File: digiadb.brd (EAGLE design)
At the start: 18.2 x 19 mm, 3 parts

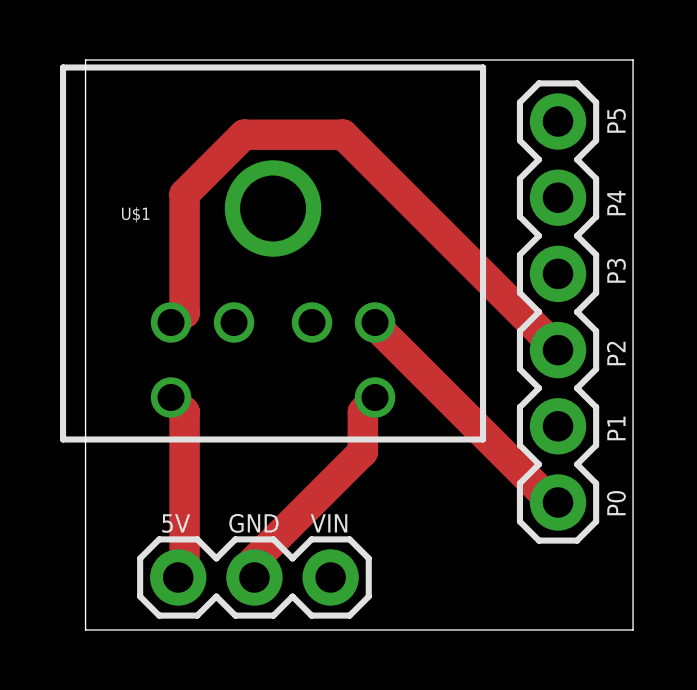
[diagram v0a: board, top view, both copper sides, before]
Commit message: added missing 470Ω pullup resistor from adb
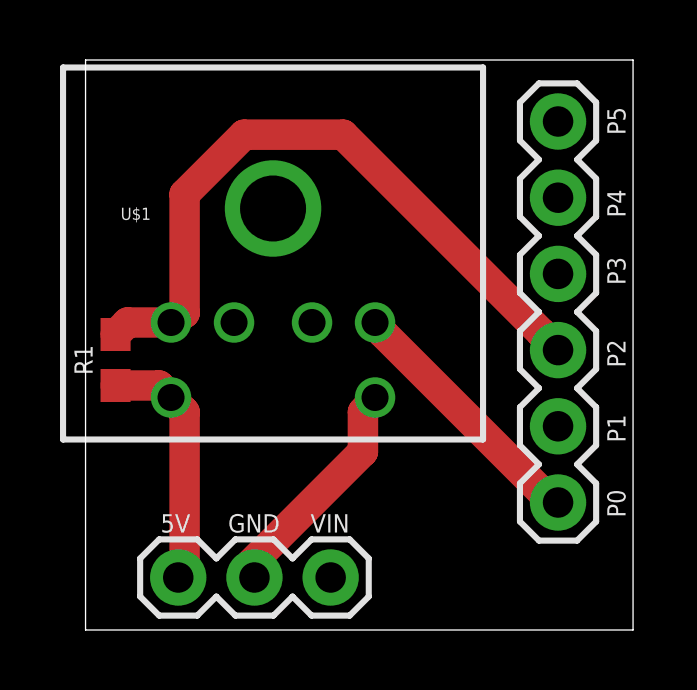
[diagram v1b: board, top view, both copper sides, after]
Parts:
- added R1: 470, SparkFun-Resistors:0603
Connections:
- net GND1 renamed GND
- net 5VCC: now also R1.1
- net ADB: now also R1.2
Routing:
- net 5VCC: track 6.26 -> 8.28 mm
- net ADB: track 20.8 -> 22.8 mm
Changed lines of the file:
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@@
 <?xml version="1.0" encoding="utf-8"?>
 <!DOCTYPE eagle SYSTEM "eagle.dtd">
-<eagle version="7.2.0">
+<eagle version="9.0.1">
 <drawing>
 <settings>
-<setting alwaysvectorfont="no"/>
+<setting alwaysvectorfont="yes"/>
+<setting keepoldvectorfont="yes"/>
 <setting verticaltext="up"/>
 </settings>
@@
 <layers>
 <layer number="1" name="Top" color="4" fill="1" visible="yes" active="yes"/>
+<layer number="2" name="Route2" color="1" fill="3" visible="yes" active="yes"/>
+<layer number="3" name="Route3" color="4" fill="3" visible="yes" active="yes"/>
+<layer number="4" name="Route4" color="1" fill="4" visible="yes" active="yes"/>
+<layer number="5" name="Route5" color="4" fill="4" visible="yes" active="yes"/>
+<layer number="6" name="Route6" color="1" fill="8" visible="yes" active="yes"/>
+<layer number="7" name="Route7" color="4" fill="8" visible="yes" active="yes"/>
+<layer number="8" name="Route8" color="1" fill="2" visible="yes" active="yes"/>
+<layer number="9" name="Route9" color="4" fill="2" visible="yes" active="yes"/>
+<layer number="10" name="Route10" color="1" fill="7" visible="yes" active="yes"/>
+<layer number="11" name="Route11" color="4" fill="7" visible="yes" active="yes"/>
+<layer number="12" name="Route12" color="1" fill="5" visible="yes" active="yes"/>
+<layer number="13" name="Route13" color="4" fill="5" visible="yes" active="yes"/>
+<layer number="14" name="Route14" color="1" fill="6" visible="yes" active="yes"/>
+<layer number="15" name="Route15" color="4" fill="6" visible="yes" active="yes"/>
 <layer number="16" name="Bottom" color="1" fill="1" visible="yes" active="yes"/>
 <layer number="17" name="Pads" color="2" fill="1" visible="yes" active="yes"/>
@@
 <param name="dpMaxLengthDifference" value="10mm"/>
 <param name="dpGapFactor" value="2.5"/>
-<param name="checkGrid" value="0"/>
 <param name="checkAngle" value="0"/>
 <param name="checkFont" value="1"/>
 <param name="checkRestrict" value="1"/>
+<param name="checkStop" value="0"/>
+<param name="checkValues" value="0"/>
 <param name="useDiameter" value="13"/>
 <param name="maxErrors" value="50"/>
@@
 </element>
 <element name="U$1" library="SparkFun-Connectors" package="MINI-DIN6" value="MINI-DIN6PTH" x="6.25" y="18.75"/>
+<element name="R1" library="SparkFun-Resistors" library_urn="urn:adsk.eagle:library:532" package="0603" package3d_urn="urn:adsk.eagle:package:39650/1" value="470" x="1" y="9" rot="R90">
+<attribute name="PROD_ID" value="RES-07869" x="1" y="9" size="1.778" layer="27" rot="R90" display="off"/>
+</element>
 </elements>
 <signals>
 <signal name="N$13">
 </signal>
-<signal name="GND1">
+<signal name="GND">
 <contactref element="U$1" pad="6"/>
 <contactref element="JP2" pad="2"/>
@@
 <wire x1="3.302" y1="7.2644" x2="2.85" y2="7.75" width="1.016" layer="1"/>
 <wire x1="3.302" y1="1.9812" x2="3.09" y2="1.75" width="1.016" layer="1"/>
+<contactref element="R1" pad="1"/>
+<wire x1="1" y1="8.15" x2="2.45" y2="8.15" width="1.016" layer="1"/>
+<wire x1="2.45" y1="8.15" x2="2.85" y2="7.75" width="1.016" layer="1"/>
 </signal>
 <signal name="POWER.ON">
@@
 <wire x1="3.302" y1="10.5664" x2="2.85" y2="10.25" width="1.016" layer="1"/>
 <wire x1="15.1892" y1="9.906" x2="15.75" y2="9.33" width="1.016" layer="1"/>
+<contactref element="R1" pad="2"/>
+<wire x1="1" y1="9.85" x2="1.4" y2="10.25" width="1.016" layer="1"/>
+<wire x1="1.4" y1="10.25" x2="2.85" y2="10.25" width="1.016" layer="1"/>
 </signal>
 </signals>
 </board>
 </drawing>
+<compatibility>
+<note version="8.2" severity="warning">
+Since Version 8.2, EAGLE supports online libraries. The ids
+of those online libraries will not be understood (or retained)
+with this version.
+</note>
+<note version="8.3" severity="warning">
+Since Version 8.3, EAGLE supports URNs for individual library
+assets (packages, symbols, and devices). The URNs of those assets
+will not be understood (or retained) with this version.
+</note>
+<note version="8.3" severity="warning">
+Since Version 8.3, EAGLE supports the association of 3D packages
+with devices in libraries, schematics, and board files. Those 3D
+packages will not be understood (or retained) with this version.
+</note>
+</compatibility>
 </eagle>
